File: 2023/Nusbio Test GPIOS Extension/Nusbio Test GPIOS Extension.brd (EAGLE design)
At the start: 44 x 50 mm, 7 parts

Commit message: Test Esxtension
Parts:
- removed GPIO_OUT: PINHD-1X10, adafruit:1X10-BIG
- removed SPI_SOIC_8_FLASH: 25AA080SN, microchip:SO-08
- removed USE_CS_3, USE_CS_4: (no value), microbuilder:SOLDERJUMPER_REFLOW
- added GPIO_0_4_CONN, GPIO_1_5_CONN, GPIO_2_6_CONN, GPIO_3_7_CONN: (no value), microbuilder:SOLDERJUMPER_REFLOW
- added LED_0, LED_1, LED_2, LED_3: (no value), adafruit:1206
- added R_2K1, R_2K2, R_2K3, R_2K4: (no value), adafruit:R1206
- moved LED_POWER 18.4 mm to (3.87, 35.0)
- moved R_4K 6.84 mm to (4.17, 30.9)
- moved GPIO_IN 0.40 mm to (22.1, 2.09)
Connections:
- removed net CS: SPI_SOIC_8_FLASH.1, USE_CS_3.2, USE_CS_4.2
- removed net CS_3: GPIO_IN.4, GPIO_OUT.4, USE_CS_3.1
- removed net CS_4: GPIO_IN.5, GPIO_OUT.5, USE_CS_4.1
- removed net GPIO8: GPIO_IN.8, GPIO_OUT.8
- removed net MISO: GPIO_IN.3, GPIO_OUT.3, SPI_SOIC_8_FLASH.2
- removed net MOSI: GPIO_IN.2, GPIO_OUT.2, SPI_SOIC_8_FLASH.5
- removed net SCK: GPIO_IN.1, GPIO_OUT.1, SPI_SOIC_8_FLASH.6
- new net GPIO0: GPIO_0_4_CONN.1, GPIO_IN.1, LED_0.A
- new net GPIO1: GPIO_1_5_CONN.1, GPIO_IN.2, LED_1.A
- new net GPIO2: GPIO_2_6_CONN.1, GPIO_IN.3, LED_2.A
- new net GPIO3: GPIO_3_7_CONN.1, GPIO_IN.4, LED_3.A
- new net GPIO4: GPIO_0_4_CONN.2, GPIO_IN.5
- new net GPIO5: GPIO_1_5_CONN.2, GPIO_IN.6
- new net N$1: LED_0.C, R_2K1.2
- new net N$3: LED_1.C, R_2K2.2
- new net N$4: LED_2.C, R_2K3.2
- new net N$5: LED_3.C, R_2K4.2
- net GND: now also R_2K1.1, R_2K2.1, R_2K3.1, R_2K4.1; no longer GPIO_OUT.10, SPI_SOIC_8_FLASH.4
- net GPIO6: now also GPIO_2_6_CONN.2, GPIO_IN.7; no longer GPIO_IN.6, GPIO_OUT.6
- net GPIO7: now also GPIO_3_7_CONN.2, GPIO_IN.8; no longer GPIO_IN.7, GPIO_OUT.7
- net VCC: no longer GPIO_OUT.9, SPI_SOIC_8_FLASH.3, SPI_SOIC_8_FLASH.7, SPI_SOIC_8_FLASH.8
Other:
- board text added: "C:/DVT/Fred.PCB/2023/Nusbio Test GPIOS Extension/Title.Logo.Gray.bmp"
- board text added: "G 0"
- board text added: "G 1"
- board text added: "G 2"
- board text added: "G 3"
- board text added: "G 4"
- board text added: "G 5"
- board text added: "G 6"
- board text added: "G 7"
- board text added: "PCBv2 - 2023.04"
- board text added: "POWER"
- board text removed: "0 CLCK"
- board text removed: "1 MOSI"
- board text removed: "2 MISO"
- board text removed: "3 CS"
- board text removed: "4 CS"
- board text removed: "5 CS"
- board text removed: "6 CS"
- board text removed: "7 CS"
- board text removed: "CLK"
- board text removed: "CS"
- board text removed: "HOLD"
- board text removed: "MISO"
- board text removed: "MOSI"
- board text removed: "PCBv2 - 2023.03"
- board text removed: "WP"

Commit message: Test Esxtension
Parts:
- moved LED_POWER 18.0 mm to (21.9, 36.0)
- moved GPIO_0_4_CONN 1.00 mm to (38.0, 12.0)
- moved GPIO_1_5_CONN 1.00 mm to (28.0, 12.0)
- moved GPIO_2_6_CONN 1.00 mm to (18.0, 12.0)
- moved GPIO_3_7_CONN 1.00 mm to (7.29, 11.7)
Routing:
- net GND: track 0.00 -> 51.3 mm
- net GPIO3: track 0.00 -> 48.3 mm, vias 0 -> 1
- net VCC: track 0.00 -> 38.1 mm, vias 0 -> 1
- net GPIO0: track 0.00 -> 37.2 mm
- net GPIO2: track 0.00 -> 30.2 mm, vias 0 -> 1
- net GPIO1: track 0.00 -> 26.8 mm, vias 0 -> 1
- net N$2: track 0.00 -> 19.8 mm
- net GPIO4: track 0.00 -> 18.0 mm
- net GPIO7: track 0.00 -> 13.4 mm
- net GPIO5: track 0.00 -> 12.6 mm
- net GPIO6: track 0.00 -> 10.3 mm
- net N$3: track 0.00 -> 4.49 mm
- net N$5: track 0.00 -> 4.41 mm
- net N$1: track 0.00 -> 4.31 mm
- net N$4: track 0.00 -> 4.20 mm

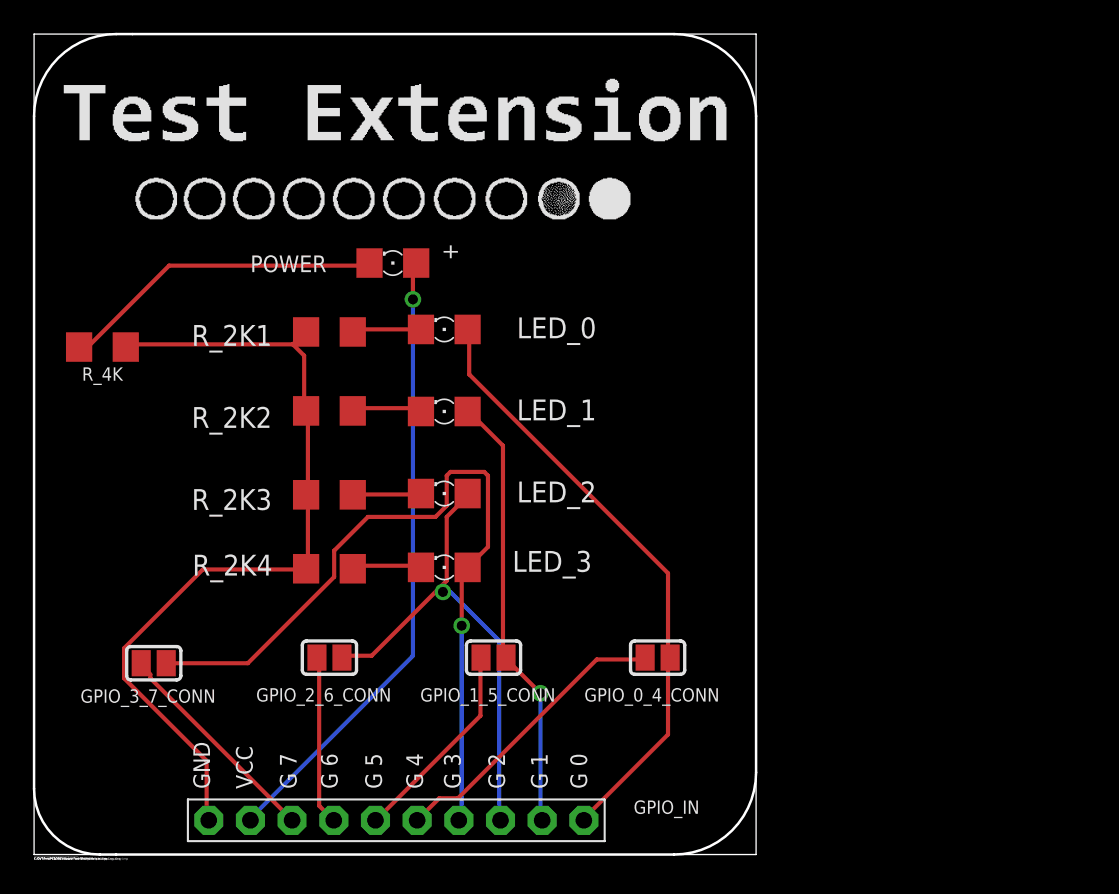
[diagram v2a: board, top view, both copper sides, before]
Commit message: Nusbio test extension
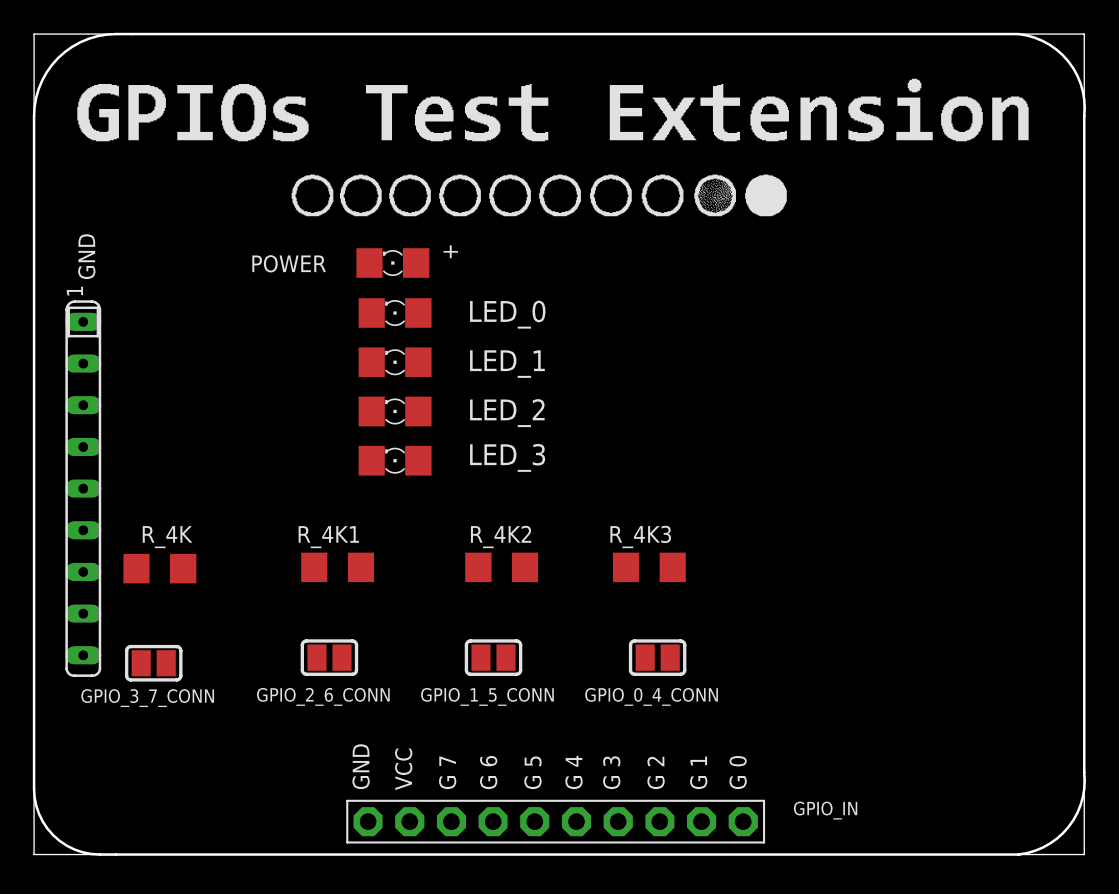
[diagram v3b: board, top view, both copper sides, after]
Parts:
- removed R_2K1, R_2K2, R_2K3, R_2K4: (no value), adafruit:R1206
- added R_4K1, R_4K2, R_4K3: (no value), adafruit:R1206
- added R_ARRAY: (no value), resistor-sip:SIP9
- moved R_4K 13.9 mm to (7.67, 17.4), turned to 0 degrees
- moved GPIO_IN 9.71 mm to (31.8, 2.00)
- moved LED_3 7.16 mm to (22.0, 24.0)
- moved LED_2 5.83 mm to (22.0, 27.0)
- moved LED_1 4.24 mm to (22.0, 30.0)
- moved LED_0 3.16 mm to (22.0, 33.0)
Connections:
- removed net N$5: LED_3.C, R_2K4.2
- new net R_LED_0: LED_0.C, R_ARRAY.2
- new net R_LED_1: LED_1.C, R_ARRAY.3
- new net R_LED_2: LED_2.C, R_ARRAY.4
- new net R_LED_3: LED_3.C, R_ARRAY.5
- new net R_LED_PWR: LED_POWER.C, R_ARRAY.6
- net GND: now also R_ARRAY.1; no longer R_2K1.1, R_2K2.1, R_2K3.1, R_2K4.1, R_4K.1
- net GPIO4: now also R_4K3.2; no longer GPIO_0_4_CONN.2
- net GPIO5: now also R_4K2.2; no longer GPIO_1_5_CONN.2
- net GPIO6: now also R_4K1.2; no longer GPIO_2_6_CONN.2
- net GPIO7: now also R_4K.2; no longer GPIO_3_7_CONN.2
- net N$1: now also GPIO_3_7_CONN.2, R_4K.1; no longer LED_0.C, R_2K1.2
- net N$2: now also GPIO_2_6_CONN.2, R_4K1.1; no longer LED_POWER.C, R_4K.2
- net N$3: now also GPIO_1_5_CONN.2, R_4K2.1; no longer LED_1.C, R_2K2.2
- net N$4: now also GPIO_0_4_CONN.2, R_4K3.1; no longer LED_2.C, R_2K3.2
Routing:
- net GND: track 51.3 -> 0.00 mm
- net GPIO3: track 48.3 -> 0.00 mm, vias 1 -> 0
- net VCC: track 38.1 -> 0.00 mm, vias 1 -> 0
- net GPIO0: track 37.2 -> 0.00 mm
- net GPIO2: track 30.2 -> 0.00 mm, vias 1 -> 0
- net GPIO1: track 26.8 -> 0.00 mm, vias 1 -> 0
- net N$2: track 19.8 -> 0.00 mm
- net GPIO4: track 18.0 -> 0.00 mm
- net GPIO7: track 13.4 -> 0.00 mm
- net GPIO5: track 12.6 -> 0.00 mm
- net GPIO6: track 10.3 -> 0.00 mm
- net N$3: track 4.49 -> 0.00 mm
- net N$5: track 4.41 -> 0.00 mm
- net N$1: track 4.31 -> 0.00 mm
- net N$4: track 4.20 -> 0.00 mm
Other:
- board size 44 x 50 mm -> 64 x 50 mm
- board text removed: "C:/DVT/Fred.PCB/2023/MadeInTheUSB.Logo.Gray.50.bmp"
- board text removed: "C:/DVT/Fred.PCB/2023/Nusbio Flash Extension/MadeInTheUSB.Logo.Gray.bmp"
- board text removed: "C:/DVT/Fred.PCB/2023/Nusbio Flash Extension/Title.Logo.Gray.bmp"
- board text removed: "C:/DVT/Fred.PCB/2023/Nusbio Test GPIOS Extension/Title.Logo.Gray.bmp"

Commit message: Nusbio test extension
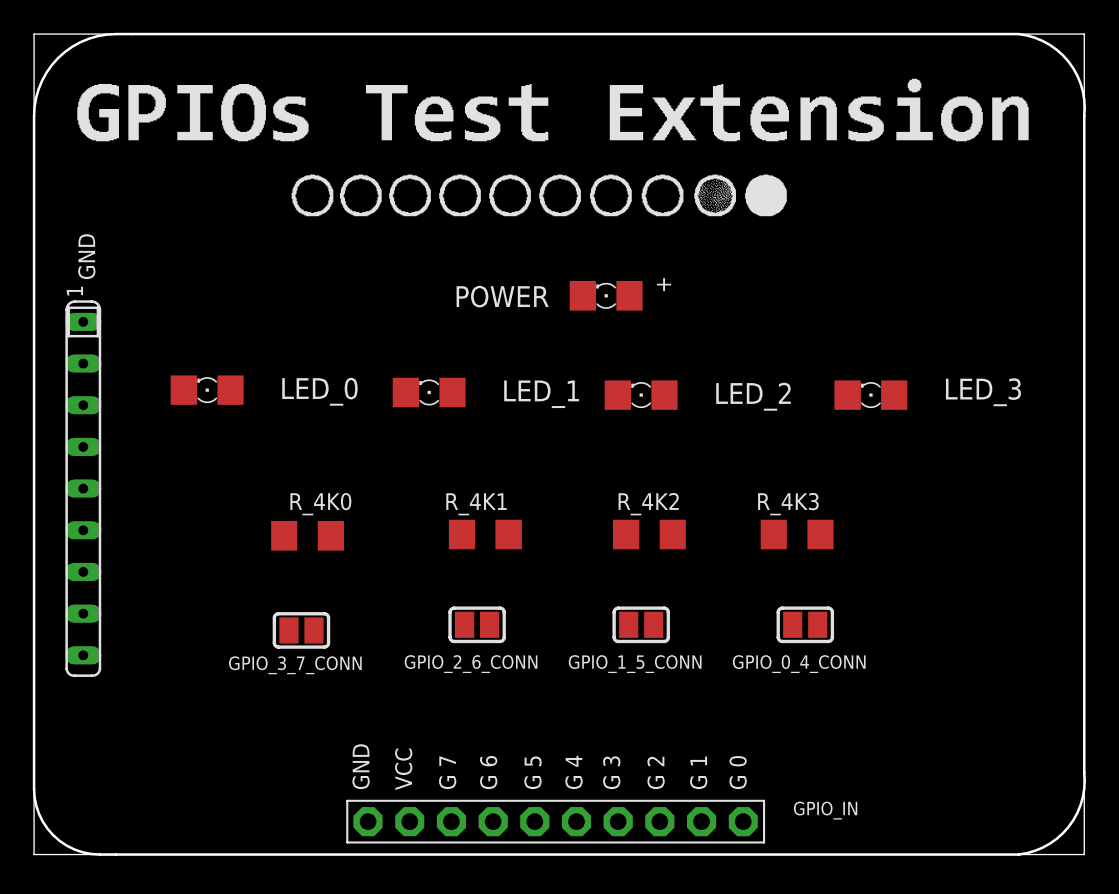
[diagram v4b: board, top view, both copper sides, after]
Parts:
- removed R_4K: (no value), adafruit:R1206
- added R_4K0: (no value), adafruit:R1206
- moved LED_3 29.3 mm to (51.0, 28.0)
- moved LED_2 15.0 mm to (37.0, 28.0)
- moved LED_POWER 13.2 mm to (34.9, 34.0)
- moved LED_0 12.4 mm to (10.6, 28.3)
- moved GPIO_0_4_CONN 9.22 mm to (47.0, 14.0)
- moved GPIO_1_5_CONN 9.22 mm to (37.0, 14.0)
- moved GPIO_2_6_CONN 9.22 mm to (27.0, 14.0)
- moved GPIO_3_7_CONN 9.22 mm to (16.3, 13.7)
- moved R_4K1 9.22 mm to (27.5, 19.5)
- moved R_4K2 9.22 mm to (37.5, 19.5)
- moved R_4K3 9.22 mm to (46.5, 19.5)
- moved LED_1 2.78 mm to (24.1, 28.2)
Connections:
- net GPIO7: now also R_4K0.2; no longer R_4K.2
- net N$1: now also R_4K0.1; no longer R_4K.1

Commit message: Finishh and send board for summer 2023 to jlpcb
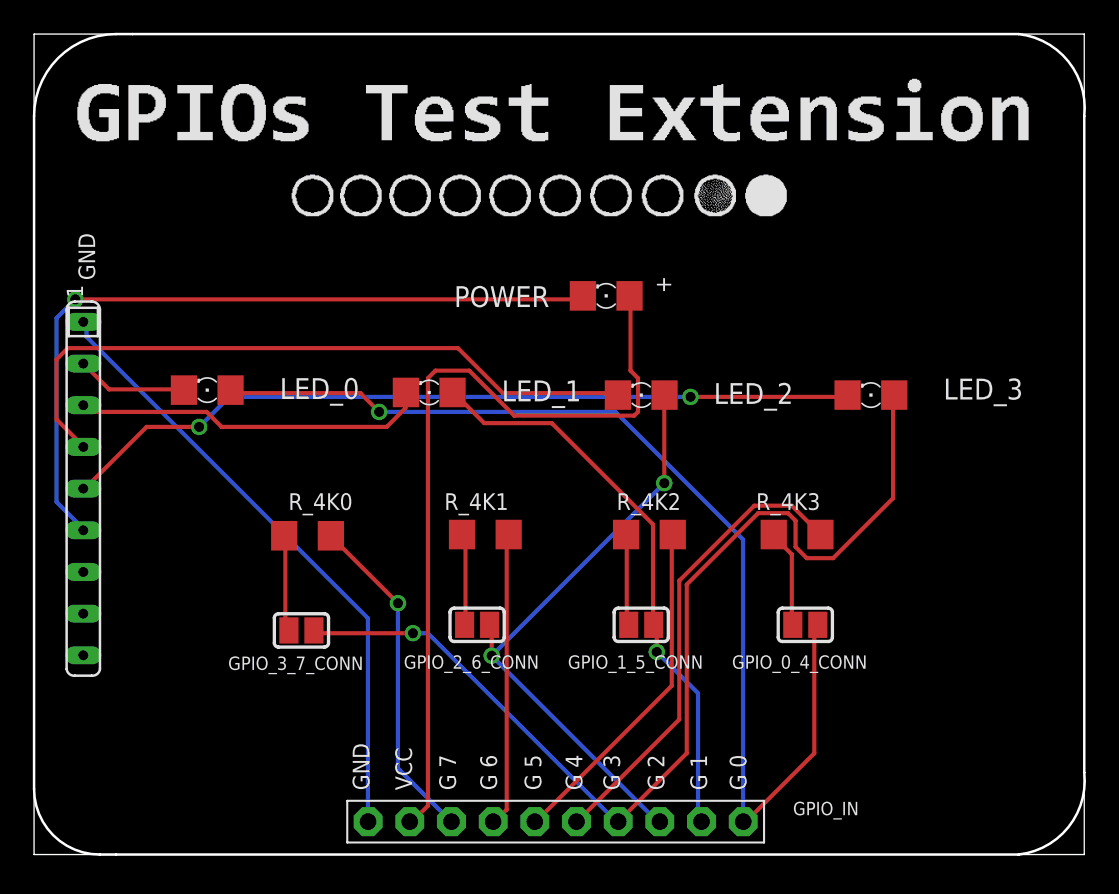
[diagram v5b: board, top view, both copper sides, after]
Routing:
- net GPIO0: track 0.00 -> 66.2 mm, vias 0 -> 1
- net GPIO3: track 0.00 -> 63.8 mm, vias 0 -> 1
- net VCC: track 0.00 -> 49.0 mm
- net R_LED_3: track 0.00 -> 48.9 mm, vias 0 -> 2
- net R_LED_PWR: track 0.00 -> 46.3 mm, vias 0 -> 1
- net R_LED_2: track 0.00 -> 41.7 mm
- net GND: track 0.00 -> 37.6 mm
- net GPIO2: track 0.00 -> 36.6 mm, vias 0 -> 2
- net GPIO1: track 0.00 -> 35.0 mm, vias 0 -> 1
- net GPIO4: track 0.00 -> 28.5 mm
- net R_LED_1: track 0.00 -> 21.6 mm
- net GPIO5: track 0.00 -> 21.0 mm
- net GPIO7: track 0.00 -> 20.5 mm, vias 0 -> 1
- net GPIO6: track 0.00 -> 17.9 mm
- net R_LED_0: track 0.00 -> 6.79 mm
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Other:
- board text added: "PCBv1 - 2023.04"
- board text removed: "PCBv2 - 2023.04"
